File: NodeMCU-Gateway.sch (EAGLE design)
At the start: 24 parts, among them J2 GROVE-I2C, J3 Lipo Battery, J4 GROVE-I2C, J5 CON_HEADER_1X08-PTH, P1 PADSMALL, P2 PADNORMAL

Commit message: Version 1.1
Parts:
- removed SJ1: JUMPER, SparkFun-Passives:JUMPER-PAD-2-NOYES_SILK
- added R3: 10K, _c2h:RESISTOR0805-RES
- added SJPWR: JUMPER-PAD-3-NOYES_SILK, SparkFun-Passives:JUMPER-PAD-3-NOYES_SILK
- WS2812-1: device _c2h:WS2812BLONG -> _c2h:WS2812B5MM
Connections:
- new net N$2: J5.4, SJPWR.2
- net 3V3: now also R3.2, SJLED.3; no longer SJLED.1
- net DIN-2: no longer SJ1.2
- net GPIO0: no longer SJ1.1
- net GPIO2: now also R3.1, U$2.SEL, U$3.SEL; no longer U$2.IRQ, U$3.DIO0
- net RST: now also SJPWR.3; no longer J5.4
- net SS: now also U$2.IRQ, U$3.DIO0; no longer U$2.SEL, U$3.SEL
- net VIN: now also SJLED.1, SJPWR.1; no longer SJLED.3
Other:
- note added: "SS"
- note removed: "GPIO15"

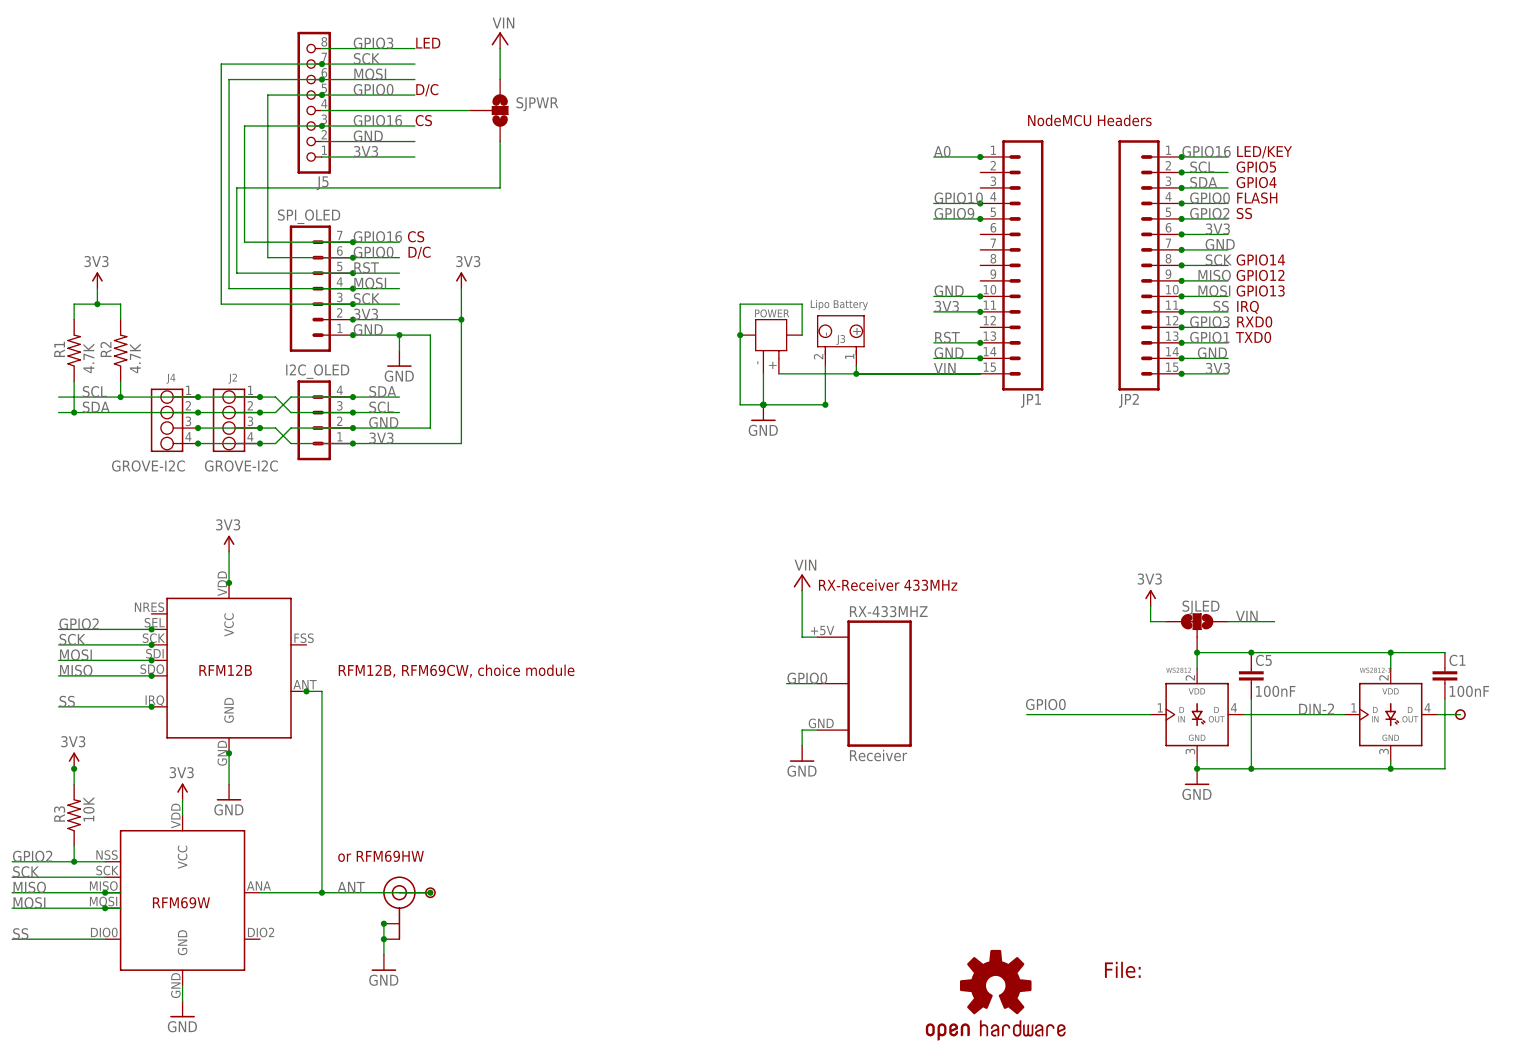
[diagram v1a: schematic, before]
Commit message: Added Footprint for ATSHA204
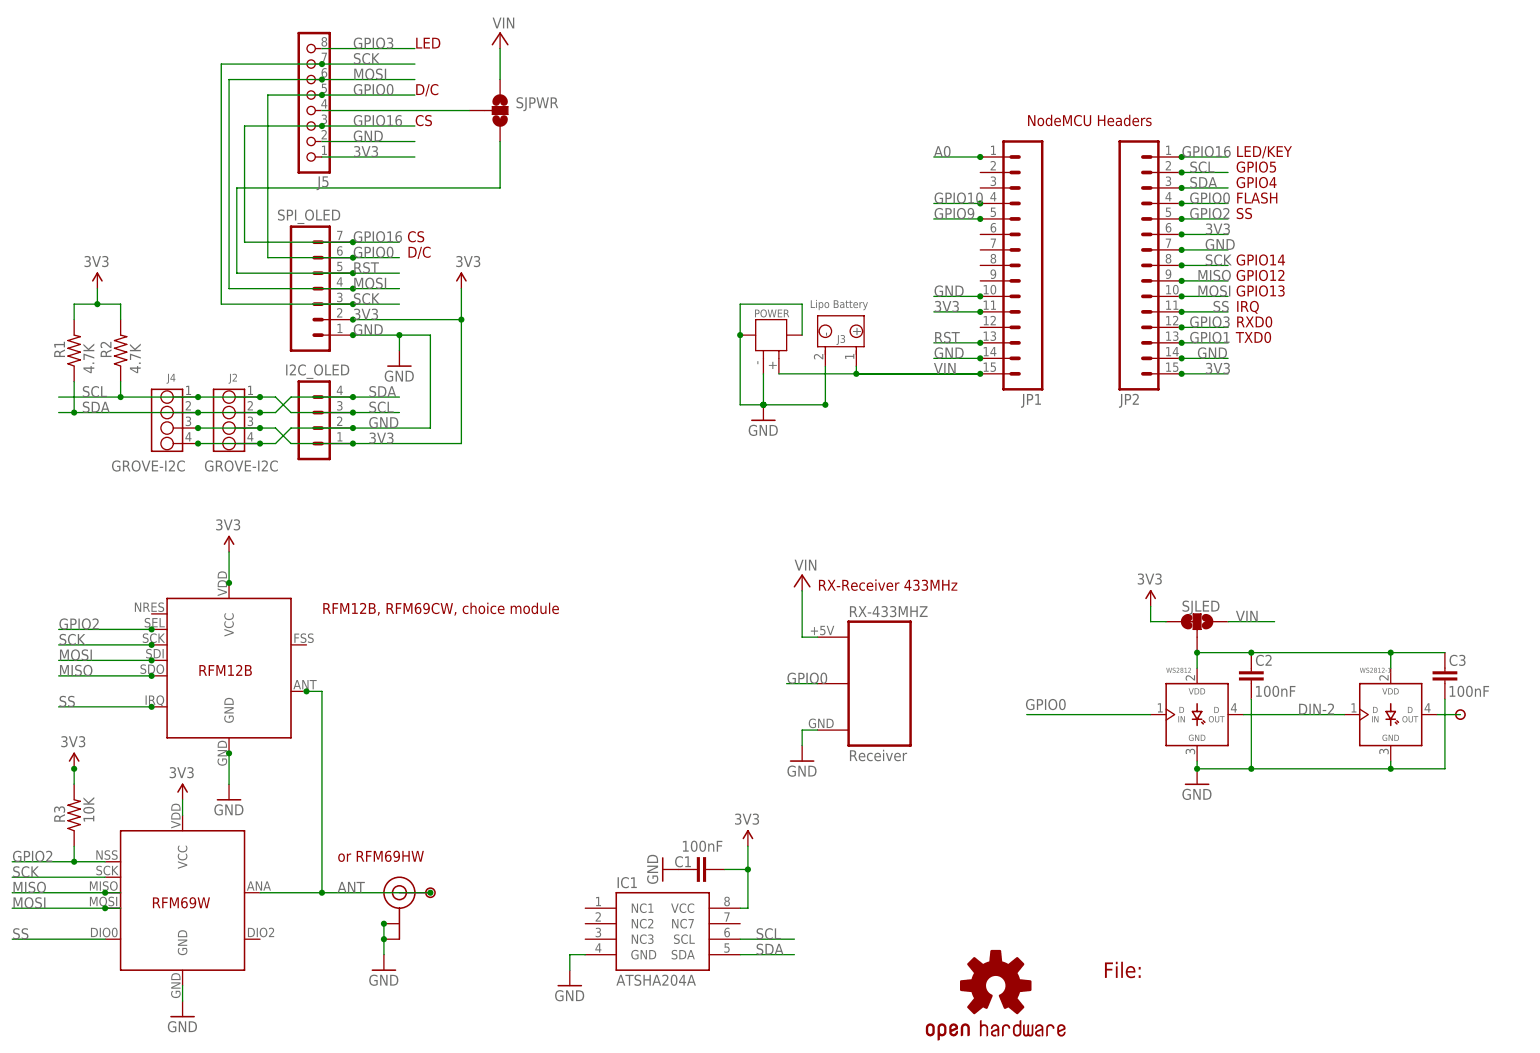
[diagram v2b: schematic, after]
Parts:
- added C3: 100nF, _c2h:CAP0805-CAP
- added IC1: ATSHA204A, SparkFun-DigitalIC:ATSHA204_SOIC8
- renumbered C5 to C2
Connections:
- net 3V3: now also C1.2, IC1.VCC
- net GND: now also C3.1, IC1.GND
- net SCL: now also IC1.SCL
- net SDA: now also IC1.SDA
- net VLED: now also C3.2; no longer C1.2
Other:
- moved on the sheet: C1

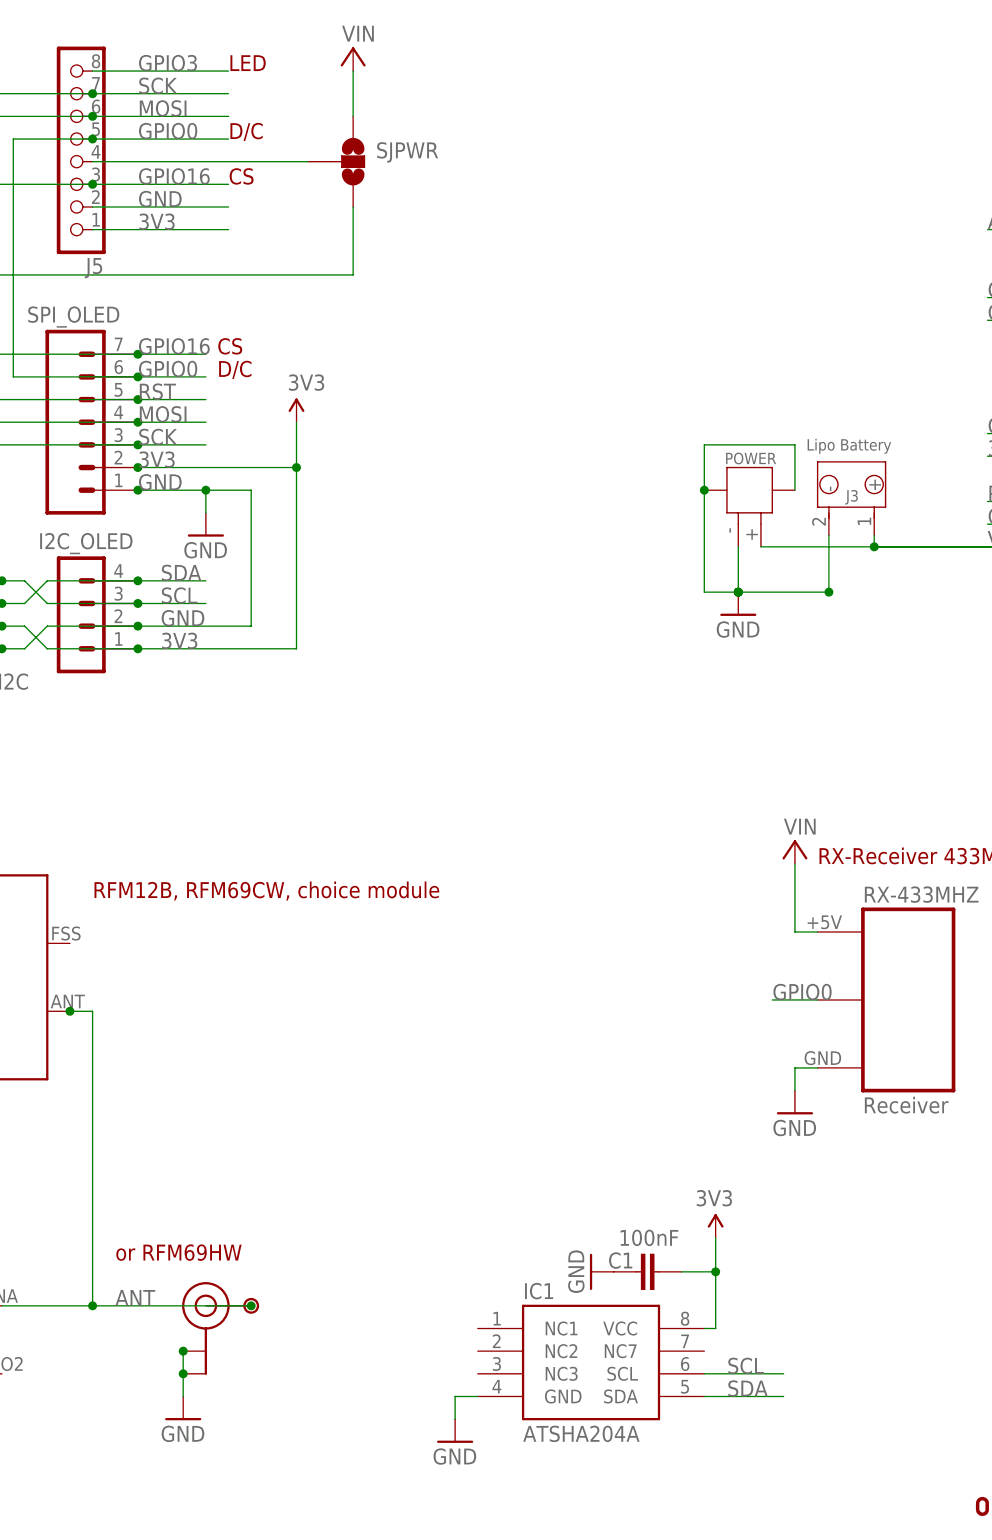
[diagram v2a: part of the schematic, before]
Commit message: Adjust SMA and UFL connectors
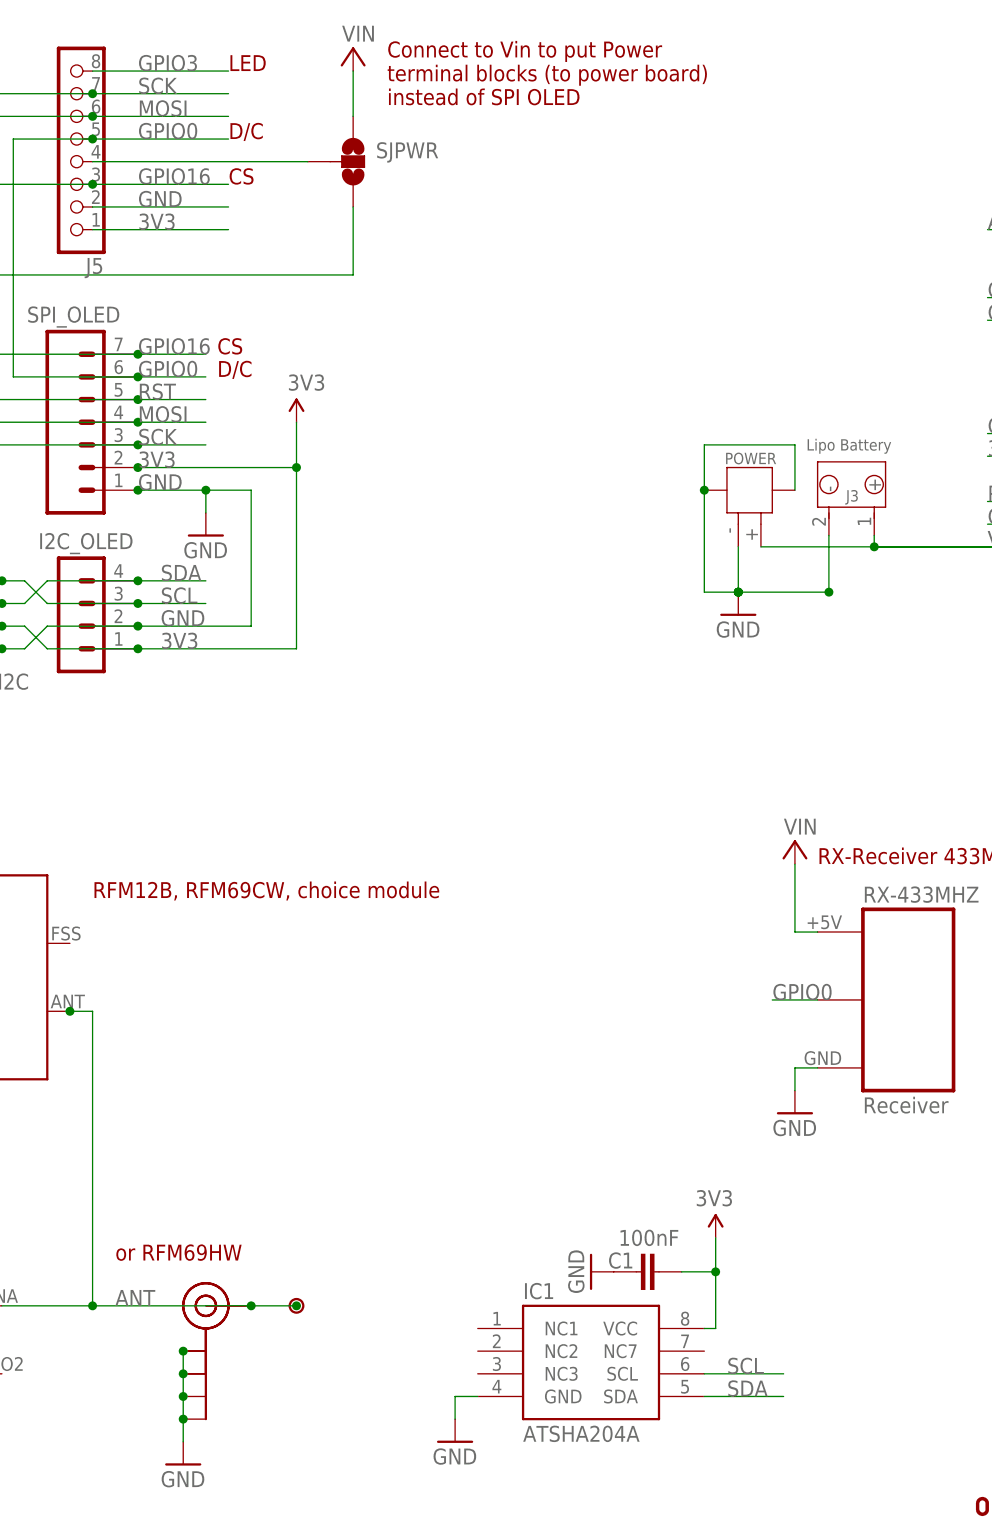
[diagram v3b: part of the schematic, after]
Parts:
- added J$1: SMA_EDGE, SparkFun-Connectors:SMA_EDGE
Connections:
- net ANT: now also J$1.SIGNAL
- net GND: now also J$1.GND@0, J$1.GND@1, J$1.GND@2, J$1.GND@3
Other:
- note added: "Connect to Vin to put Power terminal blocks (to power board) instead of SPI OLED"
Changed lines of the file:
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@@
 <setting verticaltext="up"/>
 </settings>
-<grid distance="0.05" unitdist="inch" unit="inch" style="lines" multiple="1" display="yes" altdistance="0.01" altunitdist="inch" altunit="inch"/>
+<grid distance="0.1" unitdist="inch" unit="inch" style="lines" multiple="1" display="no" altdistance="0.01" altunitdist="inch" altunit="inch"/>
 <layers>
 <layer number="1" name="Top" color="4" fill="1" visible="no" active="no"/>
@@
 <part name="C1" library="_c2h" deviceset="CAP" device="0805-CAP" value="100nF"/>
 <part name="GND5" library="supply1" deviceset="GND" device=""/>
+<part name="J$1" library="SparkFun-Connectors" deviceset="SMA_EDGE" device=""/>
 </parts>
 <sheets>
@@
 <text x="210.82" y="151.13" size="1.778" layer="94">LED/KEY</text>
 <text x="176.53" y="156.21" size="1.778" layer="94">NodeMCU Headers</text>
+<text x="93.98" y="165.1" size="1.778" layer="94">Connect to Vin to put Power
+terminal blocks (to power board)
+instead of SPI OLED</text>
 </plain>
 <instances>
@@
 <instance part="U$2" gate="G$1" x="45.72" y="68.58"/>
 <instance part="U$3" gate="G$1" x="38.1" y="27.94"/>
-<instance part="P1" gate="G$1" x="78.74" y="30.48"/>
+<instance part="P1" gate="G$1" x="83.82" y="30.48"/>
 <instance part="U-FL" gate="G$1" x="73.66" y="30.48"/>
-<instance part="GND9" gate="1" x="71.12" y="17.78"/>
+<instance part="GND9" gate="1" x="71.12" y="12.7"/>
 <instance part="GND1" gate="1" x="38.1" y="10.16"/>
 <instance part="GND13" gate="1" x="139.7" y="52.07"/>
@@
 </instance>
 <instance part="GND5" gate="1" x="116.84" y="34.29" rot="R270"/>
+<instance part="J$1" gate="1" x="73.66" y="30.48"/>
 </instances>
 <busses>
@@
 <wire x1="71.12" y1="22.86" x2="71.12" y2="20.32" width="0.1524" layer="91"/>
 <junction x="71.12" y="25.4"/>
+<pinref part="J$1" gate="1" pin="GND@0"/>
+<pinref part="J$1" gate="1" pin="GND@1"/>
+<pinref part="J$1" gate="1" pin="GND@2"/>
+<wire x1="71.12" y1="20.32" x2="71.12" y2="17.78" width="0.1524" layer="91"/>
+<junction x="71.12" y="20.32"/>
+<pinref part="J$1" gate="1" pin="GND@3"/>
+<wire x1="71.12" y1="17.78" x2="71.12" y2="15.24" width="0.1524" layer="91"/>
+<junction x="71.12" y="17.78"/>
 </segment>
 <segment>
@@
 <label x="63.5" y="30.48" size="1.778" layer="95"/>
 <pinref part="U-FL" gate="G$1" pin="SIGNAL"/>
+<junction x="83.82" y="30.48"/>
+<pinref part="J$1" gate="1" pin="SIGNAL"/>
+<wire x1="83.82" y1="30.48" x2="78.74" y2="30.48" width="0.1524" layer="91"/>
 <junction x="78.74" y="30.48"/>
 </segment>

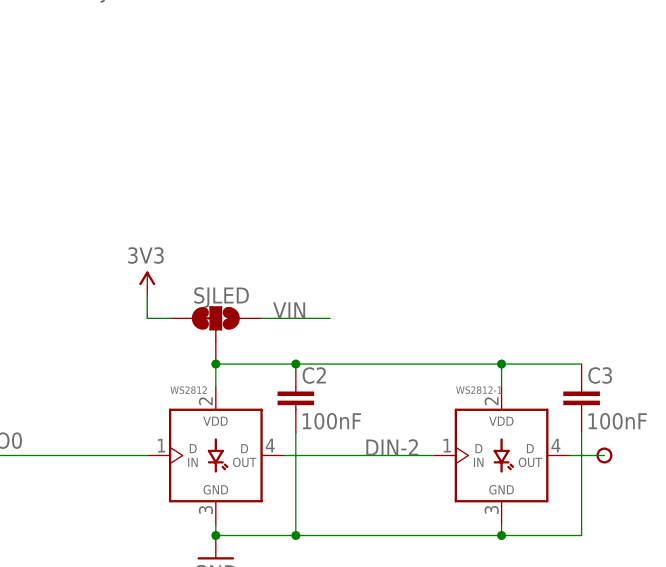
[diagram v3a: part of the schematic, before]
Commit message: Minor Silk Error
Silk SJPWR not tied to GPIO0 but RST/VIN
Increased SJPWR size for easy soldering
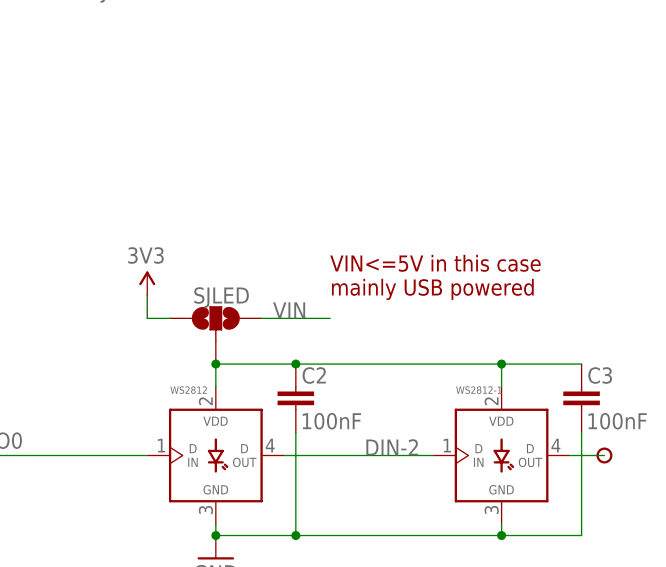
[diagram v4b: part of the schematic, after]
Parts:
- SJPWR: value JUMPER-PAD-3-NOYES_SILK -> JUMPER-PAD-3-2OF3_NC_BY_TRACE_LARGE; device SparkFun-Passives:JUMPER-PAD-3-NOYES_SILK -> SparkFun-Passives:JUMPER-PAD-3-2OF3_NC_BY_TRACE_LARGE
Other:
- note added: "VIN<=5V in this case mainly USB powered"
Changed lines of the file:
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@@
 <setting verticaltext="up"/>
 </settings>
-<grid distance="0.1" unitdist="inch" unit="inch" style="lines" multiple="1" display="no" altdistance="0.01" altunitdist="inch" altunit="inch"/>
+<grid distance="50" unitdist="mil" unit="mil" style="lines" multiple="1" display="yes" altdistance="5" altunitdist="mil" altunit="mil"/>
 <layers>
 <layer number="1" name="Top" color="4" fill="1" visible="no" active="no"/>
@@
 <part name="NAME" library="SparkFun-Aesthetics" deviceset="FRAME-A4L" device="" value="Value">
 <attribute name="CNAME" value="ESP8266 NodeMCU RF Gateway + Display"/>
-<attribute name="CREVISION" value="1.1"/>
+<attribute name="CREVISION" value="1.1a"/>
 <attribute name="DESIGNER" value="Charles-Henri Hallard"/>
 </part>
@@
 <part name="P+1" library="_c2h" deviceset="3V3-EXT" device="" value="3V3"/>
 <part name="VIN1" library="supply1" deviceset="+5V" device="" value="VIN"/>
-<part name="SJPWR" library="SparkFun-Passives" deviceset="JUMPER-PAD-3-NO" device="YES_SILK" value=""/>
+<part name="SJPWR" library="SparkFun-Passives" deviceset="JUMPER-PAD-3-2OF3_NC_BY_TRACE" device="_LARGE" value=""/>
 <part name="IC1" library="SparkFun-DigitalIC" deviceset="ATSHA204_SOIC8" device="" value="ATSHA204A"/>
 <part name="P+8" library="_c2h" deviceset="3V3-EXT" device="" value="3V3"/>
@@
 terminal blocks (to power board)
 instead of SPI OLED</text>
+<text x="217.17" y="77.47" size="1.778" layer="94">VIN&lt;=5V in this case
+mainly USB powered</text>
 </plain>
 <instances>
